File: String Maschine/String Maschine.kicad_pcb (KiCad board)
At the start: 2 copper layers, 40 parts, among them J1 Conn_01x03_Male, U1 LM358, U2 4069, U3 LM358, U4 LM317_TO-220, U5 MN3209, U6 LM7809_TO220, U7 4010

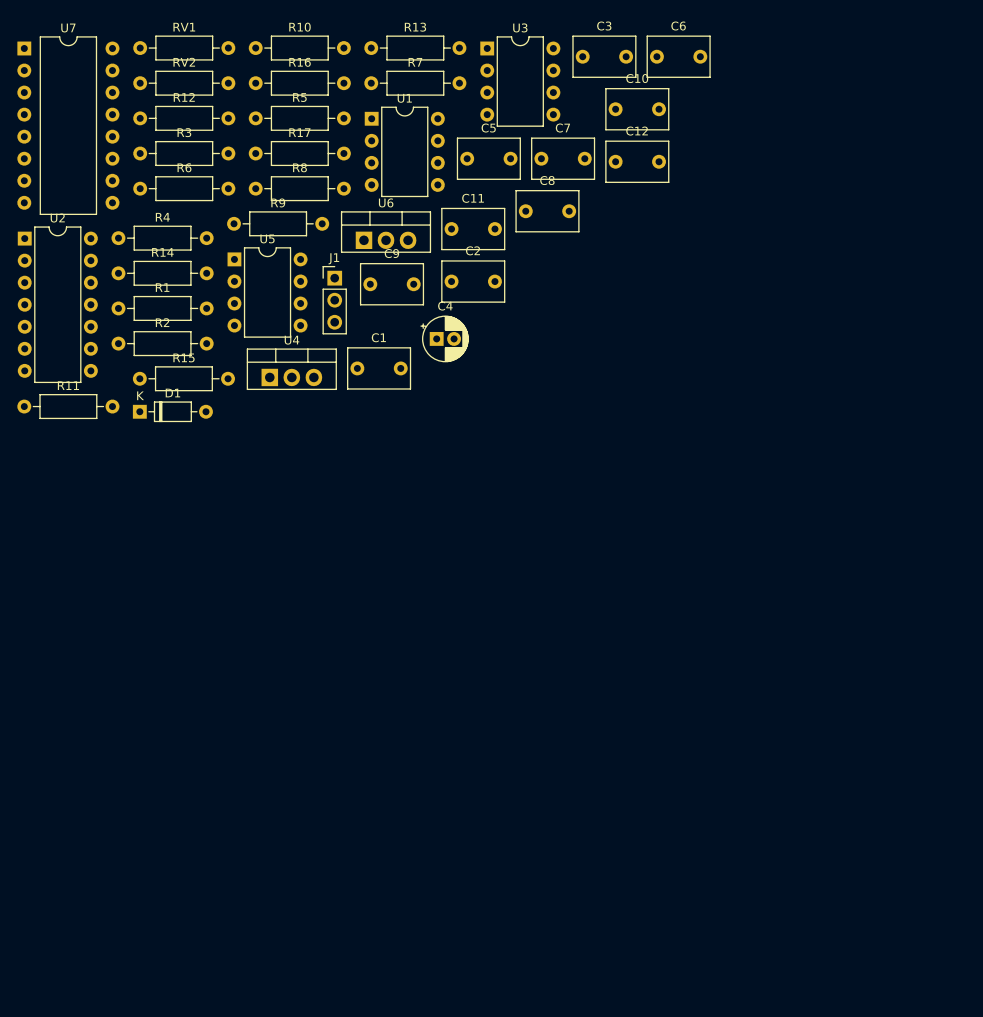
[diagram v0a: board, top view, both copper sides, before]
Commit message: String Maschine - assign symbols
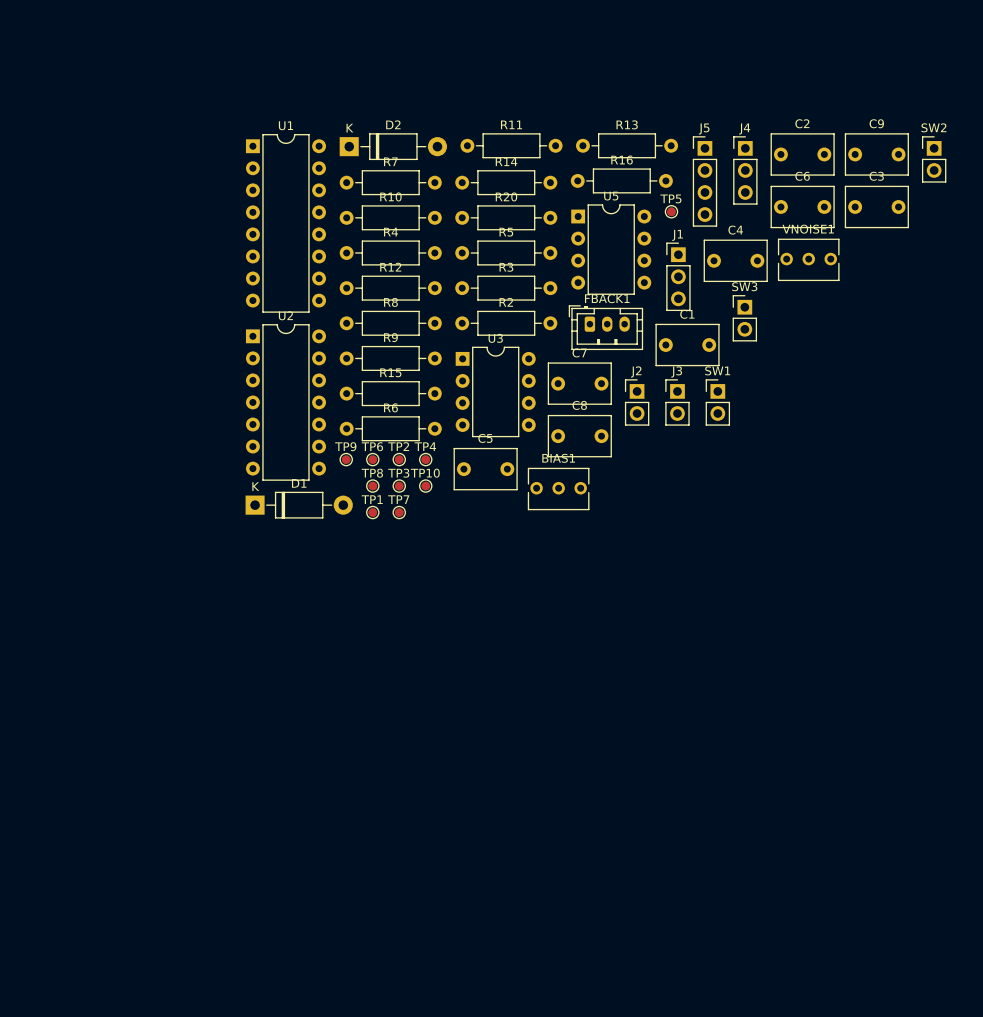
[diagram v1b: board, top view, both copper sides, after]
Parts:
- removed C10, C11: 3.3n, Capacitor_THT:C_Rect_L7.0mm_W4.5mm_P5.00mm
- removed C12: 220n, Capacitor_THT:C_Rect_L7.0mm_W4.5mm_P5.00mm
- removed R1: 10k, Resistor_THT:R_Axial_DIN0207_L6.3mm_D2.5mm_P10.16mm_Horizontal
- removed R17, RV2: 100k, Resistor_THT:R_Axial_DIN0207_L6.3mm_D2.5mm_P10.16mm_Horizontal
- removed RV1: 2k, Resistor_THT:R_Axial_DIN0207_L6.3mm_D2.5mm_P10.16mm_Horizontal
- removed U4: LM317_TO-220, Package_TO_SOT_THT:TO-220-3_Vertical
- removed U6: LM7809_TO220, Package_TO_SOT_THT:TO-220-3_Vertical
- removed U7: 4010, Package_DIP:DIP-16_W10.16mm
- added BIAS1: 100k, Potentiometer_THT:Potentiometer_Bourns_3266Y_Vertical, F.Cu at (122.5, 90.0)
- added D2: 1N47xxA, Diode_THT:D_DO-41_SOD81_P10.16mm_Horizontal, F.Cu at (95.8, 50.6)
- added FBACK1: 100k, Connector_JST:JST_PH_B3B-PH-K_1x03_P2.00mm_Vertical, F.Cu at (123.6, 71.1)
- added J2: VGG, Connector_PinHeader_2.54mm:PinHeader_1x02_P2.54mm_Vertical, F.Cu at (129.0, 78.8)
- added J3: VOut, Connector_PinHeader_2.54mm:PinHeader_1x02_P2.54mm_Vertical, F.Cu at (133.7, 78.8)
- added J4: Vin, Connector_PinHeader_2.54mm:PinHeader_1x03_P2.54mm_Vertical, F.Cu at (141.5, 50.9)
- added J5: CTLS, Connector_PinHeader_2.54mm:PinHeader_1x04_P2.54mm_Vertical, F.Cu at (136.8, 50.9)
- added R20: 10k, Resistor_THT:R_Axial_DIN0207_L6.3mm_D2.5mm_P10.16mm_Horizontal, F.Cu at (108.8, 58.9)
- added SW1: FBACK, Connector_PinHeader_2.54mm:PinHeader_1x02_P2.54mm_Vertical, F.Cu at (138.3, 78.8)
- added SW2: NOISE, Connector_PinHeader_2.54mm:PinHeader_1x02_P2.54mm_Vertical, F.Cu at (163.2, 50.9)
- added SW3: FBACK, Connector_PinHeader_2.54mm:PinHeader_1x02_P2.54mm_Vertical, F.Cu at (141.4, 69.2)
- added TP1: NIn, TestPoint:TestPoint_Pad_D1.0mm, F.Cu at (98.5, 92.8)
- added TP10: DELAY, TestPoint:TestPoint_Pad_D1.0mm, F.Cu at (104.7, 89.8)
- added TP2: VCF, TestPoint:TestPoint_Pad_D1.0mm, F.Cu at (101.6, 86.7)
- added TP3: VGG, TestPoint:TestPoint_Pad_D1.0mm, F.Cu at (101.6, 89.8)
- added TP4: VBIAS, TestPoint:TestPoint_Pad_D1.0mm, F.Cu at (104.7, 86.7)
- added TP5: CP2, TestPoint:TestPoint_Pad_D1.0mm, F.Cu at (133.0, 58.1)
- added TP6: CP1, TestPoint:TestPoint_Pad_D1.0mm, F.Cu at (98.5, 86.7)
- added TP7: CVF, TestPoint:TestPoint_Pad_D1.0mm, F.Cu at (101.6, 92.8)
- added TP8: CVN, TestPoint:TestPoint_Pad_D1.0mm, F.Cu at (98.5, 89.8)
- added TP9: GND, TestPoint:TestPoint_Pad_D1.0mm, F.Cu at (95.5, 86.7)
- added VNOISE1: 100k, Potentiometer_THT:Potentiometer_Bourns_3266Y_Vertical, F.Cu at (151.3, 63.6)
- C1: value 330n -> 220n
- C2: value 100n -> 560p
- C3: value 220n -> 470p
- C4: value 47u -> 560p; footprint Capacitor_THT:CP_Radial_D5.0mm_P2.00mm -> Capacitor_THT:C_Rect_L7.0mm_W4.5mm_P5.00mm
- C5: value 3.3n -> 470p
- C6: value 3.3n -> 560p
- C9: value 3.3n -> 1u
- D1: value BZX55C4V7 -> 1N47xxA; footprint Diode_THT:D_DO-35_SOD27_P7.62mm_Horizontal -> Diode_THT:D_DO-41_SOD81_P10.16mm_Horizontal
- J1: value Conn_01x03_Male -> Vin
- R14, R16, R5, R6: value 47k -> 27k
- R15: value 47k -> 470
- R2: value 1k -> 27k
- R3: value 10k -> 470
- R4: value 10k -> 27k
- R7: value 100k -> 470
- R8, R9: value 100k -> 27k
- U1: value LM358 -> v2164; footprint Package_DIP:DIP-8_W7.62mm -> Package_DIP:DIP-16_W7.62mm
- U2: value 4069 -> LM324
- U3: value LM358 -> Pentanoise
- moved R11 59.2 mm to (109.5, 50.5)
- moved C9 57.8 mm to (154.1, 51.5)
- moved R14 40.9 mm to (108.8, 54.8)
- moved C2 40.7 mm to (145.6, 51.5)
- moved R3 40.2 mm to (108.8, 67.0)
- moved U5 39.9 mm to (122.2, 58.7)
- moved J1 39.7 mm to (133.8, 63.1)
- moved R2 39.7 mm to (108.8, 71.0)
- moved R16 38.8 mm to (122.2, 54.6)
- moved R6 36.5 mm to (95.5, 83.2)
- moved U3 35.9 mm to (108.9, 75.1)
- moved C3 35.8 mm to (154.1, 57.6)
- moved C5 35.8 mm to (109.0, 87.8)
- moved C1 35.6 mm to (132.3, 73.5)
- moved C4 33.2 mm to (137.9, 63.8)
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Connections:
- C1 pad 1: GND -> Net-(C1-Pad1)
- C1 pad 2: +12V -> Net-(C1-Pad2)
- C2 pad 2: +9V -> Net-(C2-Pad2)
- C3 pad 1: FXIn -> Net-(C3-Pad1)
- C4 pad 1: +4V5 -> GND
- C4 pad 2: GND -> Net-(C4-Pad2)
- C5 pad 1: GND -> Net-(C5-Pad1)
- C9 pad 1: GND -> Net-(R20-Pad2)
- C9 pad 2: Net-(C9-Pad2) -> Net-(U5-Pad3)
- D1 pad 1: Net-(R2-Pad1) -> +5V
- D1 pad 2: GND -> Net-(U5-Pad3)
- J1 pad 1: Net-(J1-Pad1) -> -5V
- J1 pad 3: +3V3 -> +5V
- R14 pad 1: Net-(C8-Pad2) -> Net-(R14-Pad1)
- R14 pad 2: Net-(C9-Pad2) -> Net-(C8-Pad2)
- R15 pad 1: Net-(C9-Pad2) -> Net-(R15-Pad1)
- R15 pad 2: Net-(C10-Pad2) -> Net-(C6-Pad2)
- R16 pad 1: Net-(C10-Pad2) -> Net-(R16-Pad1)
- R16 pad 2: Net-(C11-Pad2) -> Net-(R15-Pad1)
- R2 pad 2: +9V -> Net-(C1-Pad2)
- R3 pad 1: Net-(R1-Pad2) -> Net-(R2-Pad1)
- R3 pad 2: Net-(R3-Pad2) -> Net-(C2-Pad2)
- R4 pad 1: Net-(R2-Pad1) -> Net-(R4-Pad1)
- R4 pad 2: +4V5 -> Net-(R4-Pad2)
- R5 pad 1: Net-(R3-Pad2) -> Net-(R20-Pad2)
- R5 pad 2: Net-(C5-Pad2) -> Net-(R4-Pad1)
- R6 pad 1: Net-(C5-Pad2) -> Net-(R6-Pad1)
- R6 pad 2: Net-(C6-Pad2) -> Net-(C3-Pad1)
- R7 pad 1: Net-(C6-Pad2) -> Net-(R6-Pad1)
- R7 pad 2: Net-(R7-Pad2) -> Net-(C4-Pad2)
- R8 pad 1: Net-(C6-Pad2) -> Net-(C5-Pad1)
- R8 pad 2: Net-(R8-Pad2) -> Net-(R6-Pad1)
- R9 pad 1: Net-(R7-Pad2) -> Net-(R15-Pad1)
- R9 pad 2: Net-(C7-Pad1) -> Net-(C5-Pad1)
- U1 pad 1: Net-(R3-Pad2) -> unconnected-(U1-Pad1)
- U1 pad 2: Net-(R1-Pad2) -> Net-(R15-Pad1)
- U1 pad 3: +4V5 -> CVF
- U1 pad 4: GND -> Net-(C5-Pad2)
- U1 pad 5: +4V5 -> Net-(C3-Pad2)
- U1 pad 6: Net-(C6-Pad2) -> CVF
- U1 pad 7: Net-(R8-Pad2) -> Net-(R6-Pad1)
- U1 pad 8: +9V -> GND
- U2 pad 1: CP1 -> Net-(C5-Pad1)
- U2 pad 10: unconnected-(U2-Pad10) -> GND
- U2 pad 11: GND -> -5V
- U2 pad 12: unconnected-(U2-Pad12) -> GND
- U2 pad 13: GND -> Net-(R14-Pad1)
- U2 pad 14: +9V -> Net-(C7-Pad1)
- U2 pad 2: CP2 -> Net-(C5-Pad2)
- U2 pad 4: unconnected-(U2-Pad4) -> +5V
- U2 pad 6: unconnected-(U2-Pad6) -> Net-(C3-Pad2)
- U2 pad 7: GND -> Net-(C3-Pad1)
- U2 pad 8: unconnected-(U2-Pad8) -> Net-(R20-Pad2)
- U2 pad 9: GND -> Net-(R4-Pad1)
- U3 pad 1: Net-(C12-Pad1) -> +5V
- U3 pad 2: Net-(C11-Pad2) -> unconnected-(U3-Pad2)
- U3 pad 3: +4V5 -> unconnected-(U3-Pad3)
- U3 pad 4: GND -> (no net)
- U3 pad 5: +4V5 -> unconnected-(U3-Pad5)
- U3 pad 6: Net-(C7-Pad1) -> unconnected-(U3-Pad6)
- U3 pad 7: Net-(R7-Pad2) -> Net-(VNOISE1-Pad1)
- U3 pad 8: +9V -> GND
- U5 pad 3: Net-(R8-Pad2) -> Net-(U5-Pad3)
- U5 pad 4: /+8.4V  -> VGG
- U5 pad 5: +9V -> +5V

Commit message: String Maschine - finish voice board
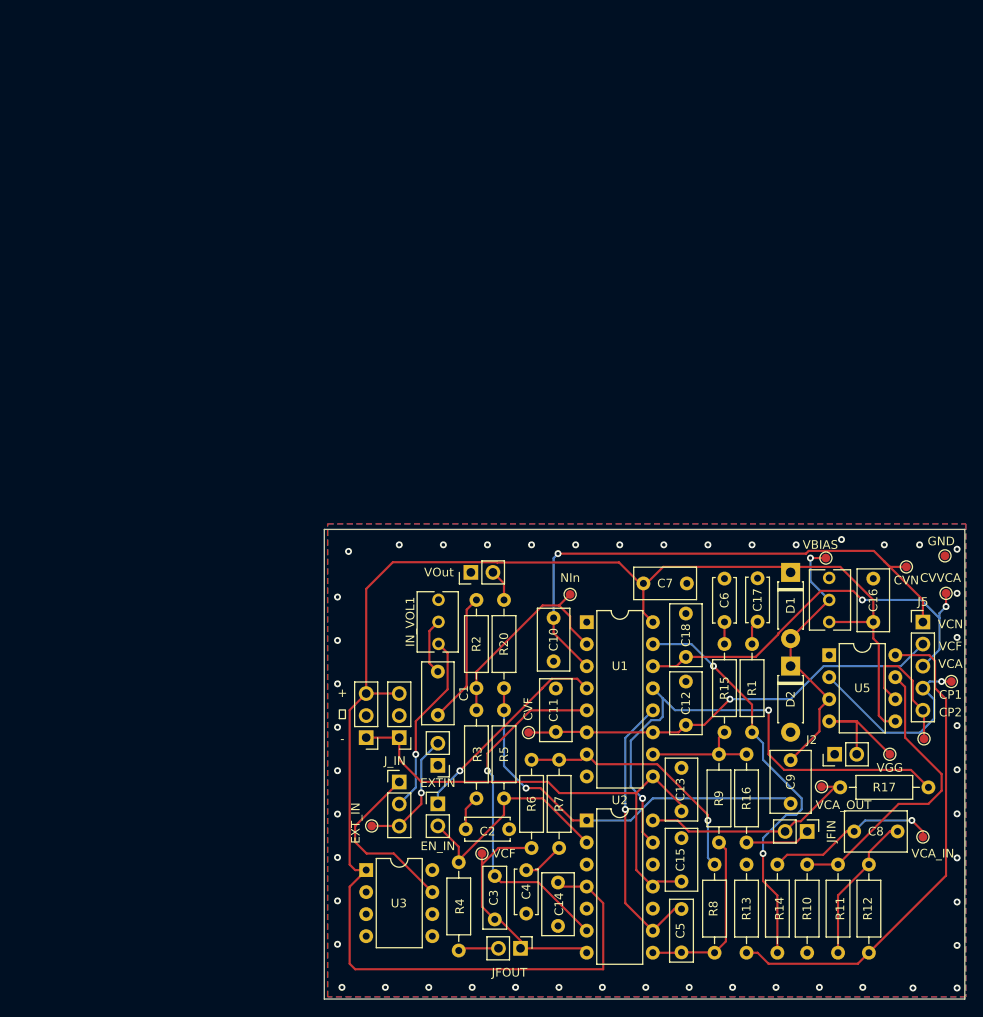
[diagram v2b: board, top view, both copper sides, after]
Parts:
- removed FBACK1: 100k, Connector_JST:JST_PH_B3B-PH-K_1x03_P2.00mm_Vertical
- removed VNOISE1: 100k, Potentiometer_THT:Potentiometer_Bourns_3266Y_Vertical
- added C10: 220n, Capacitor_THT:C_Rect_L7.0mm_W3.5mm_P5.00mm, F.Cu at (119.4, 109.9)
- added C11: 220n, Capacitor_THT:C_Rect_L7.0mm_W3.5mm_P5.00mm, F.Cu at (119.6, 113.1)
- added C12: 220n, Capacitor_THT:C_Rect_L7.0mm_W3.5mm_P5.00mm, F.Cu at (134.6, 112.3)
- added C13: 100n, Capacitor_THT:C_Rect_L7.0mm_W3.5mm_P5.00mm, F.Cu at (134.1, 127.2)
- added C14: 100n, Capacitor_THT:C_Rect_L7.0mm_W3.5mm_P5.00mm, F.Cu at (119.9, 135.4)
- added C15: 100n, Capacitor_THT:C_Rect_L7.0mm_W3.5mm_P5.00mm, F.Cu at (134.1, 135.3)
- added C16: 100n, Capacitor_THT:C_Rect_L7.0mm_W3.5mm_P5.00mm, F.Cu at (156.2, 105.4)
- added C17: 560p, Capacitor_THT:C_Disc_D5.0mm_W2.5mm_P5.00mm, F.Cu at (142.9, 100.4)
- added C18: 220n, Capacitor_THT:C_Rect_L7.0mm_W3.5mm_P5.00mm, F.Cu at (134.6, 104.4)
- added IN1: J_IN, Connector_PinHeader_2.54mm:PinHeader_1x03_P2.54mm_Vertical, F.Cu at (101.6, 123.8)
- added IN_VOL1: 100k, Potentiometer_THT:Potentiometer_Bourns_3266Y_Vertical, F.Cu at (106.1, 107.9)
- added J6: EXTIN, Connector_PinHeader_2.54mm:PinHeader_1x02_P2.54mm_Vertical, F.Cu at (106.0, 121.9)
- added R1: 470, Resistor_THT:R_Axial_DIN0207_L6.3mm_D2.5mm_P10.16mm_Horizontal, F.Cu at (142.2, 118.1)
- added R17: 27k, Resistor_THT:R_Axial_DIN0207_L6.3mm_D2.5mm_P10.16mm_Horizontal, F.Cu at (152.4, 124.5)
- added TP11: EXT_IN, TestPoint:TestPoint_Pad_D1.0mm, F.Cu at (98.4, 128.9)
- added TP12: CVVCA, TestPoint:TestPoint_Pad_D1.0mm, F.Cu at (164.6, 102.1)
- added TP13: VCA_IN, TestPoint:TestPoint_Pad_D1.0mm, F.Cu at (161.9, 130.2)
- C1: footprint Capacitor_THT:C_Rect_L7.0mm_W4.5mm_P5.00mm -> Capacitor_THT:C_Rect_L7.0mm_W3.5mm_P5.00mm
- C2, C4, C6: footprint Capacitor_THT:C_Rect_L7.0mm_W4.5mm_P5.00mm -> Capacitor_THT:C_Disc_D5.0mm_W2.5mm_P5.00mm
- C3, C5: value 470p -> 1.2n; footprint Capacitor_THT:C_Rect_L7.0mm_W4.5mm_P5.00mm -> Capacitor_THT:C_Rect_L7.0mm_W2.5mm_P5.00mm
- C7: value 220n -> 100n; footprint Capacitor_THT:C_Rect_L7.0mm_W4.5mm_P5.00mm -> Capacitor_THT:C_Rect_L7.0mm_W3.5mm_P5.00mm
- D1, D2: footprint Diode_THT:D_DO-41_SOD81_P10.16mm_Horizontal -> Diode_THT:D_DO-41_SOD81_P7.62mm_Horizontal
- J5: footprint Connector_PinHeader_2.54mm:PinHeader_1x04_P2.54mm_Vertical -> Connector_PinHeader_2.54mm:PinHeader_1x05_P2.54mm_Vertical
- SW1: value FBACK -> JFOUT
- SW2: value NOISE -> EN_IN
- SW3: value FBACK -> JFIN
- TP10: value DELAY -> VCA_OUT
- TP5: value CP2 -> CP1
- TP6: value CP1 -> CP2
- moved R10 99.9 mm to (148.6, 143.5), turned to 90 degrees
- moved R14 95.9 mm to (145.2, 143.5), turned to 90 degrees
- moved R13 94.9 mm to (141.6, 143.5), turned to 90 degrees
- moved SW2 94.7 mm to (106.0, 126.4)
- moved R11 93.2 mm to (152.1, 133.3), turned to -90 degrees
- moved C3 92.0 mm to (112.6, 139.7), turned to 90 degrees
- moved R12 89.6 mm to (155.7, 133.3), turned to -90 degrees
- moved R8 84.0 mm to (137.9, 143.5), turned to 90 degrees
- moved C2 83.8 mm to (114.3, 129.3), turned to 180 degrees
- moved J4 80.7 mm to (97.8, 118.7), turned to 180 degrees
- moved R16 78.7 mm to (141.6, 130.8), turned to 90 degrees
- moved D2 78.5 mm to (146.7, 110.5), turned to -90 degrees
- moved C4 78.2 mm to (116.2, 139.0), turned to 90 degrees
- moved C9 75.1 mm to (146.7, 126.3), turned to 90 degrees
- moved R4 71.4 mm to (108.5, 133.1), turned to -90 degrees
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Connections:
- C7 pad 1: Net-(C7-Pad1) -> GND
- C7 pad 2: Net-(C7-Pad2) -> +5V
- C9 pad 1: Net-(R20-Pad2) -> Net-(C9-Pad1)
- J5 pad 3: CP1 -> CVVCA
- J5 pad 4: CP2 -> CP1
- R14 pad 1: Net-(R14-Pad1) -> Net-(R1-Pad1)
- R20 pad 2: Net-(R20-Pad2) -> Net-(C9-Pad1)
- R5 pad 1: Net-(R20-Pad2) -> Net-(C9-Pad1)
- SW2 pad 1: Net-(U1-Pad13) -> Net-(SW2-Pad1)
- SW3 pad 2: Net-(C7-Pad2) -> Net-(R17-Pad1)
- TP10 pad 1: Net-(C7-Pad2) -> Net-(R17-Pad1)
- U1 pad 10: GND -> Net-(R15-Pad1)
- U1 pad 11: GND -> CVF
- U1 pad 12: unconnected-(U1-Pad12) -> Net-(C5-Pad2)
- U1 pad 13: Net-(U1-Pad13) -> Net-(R17-Pad2)
- U1 pad 14: CVN -> CVVCA
- U1 pad 15: Net-(R2-Pad1) -> Net-(R1-Pad1)
- U1 pad 2: Net-(R15-Pad1) -> Net-(R2-Pad1)
- U1 pad 3: CVF -> CVN
- U1 pad 4: Net-(C5-Pad2) -> Net-(SW2-Pad1)
- U2 pad 1: Net-(C5-Pad1) -> Net-(C9-Pad1)
- U2 pad 13: Net-(R14-Pad1) -> Net-(R17-Pad2)
- U2 pad 14: Net-(C7-Pad1) -> Net-(R17-Pad1)
- U2 pad 2: Net-(C5-Pad2) -> Net-(R4-Pad1)
- U2 pad 8: Net-(R20-Pad2) -> Net-(C5-Pad1)
- U2 pad 9: Net-(R4-Pad1) -> Net-(C5-Pad2)
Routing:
- net +5V: track 0.00 -> 182.7 mm
- net CVN: track 0.00 -> 64.6 mm, vias 0 -> 1
- net Net-(R17-Pad2): track 0.00 -> 59.0 mm, vias 0 -> 2
- net -5V: track 0.00 -> 58.4 mm
- net Net-(R12-Pad2): track 0.00 -> 57.8 mm
- net CVF: track 0.00 -> 49.7 mm, vias 0 -> 1
- net Net-(R1-Pad1): track 0.00 -> 48.4 mm, vias 0 -> 2
- net CVVCA: track 0.00 -> 47.5 mm, vias 0 -> 2
- net Net-(C9-Pad1): track 0.00 -> 45.9 mm, vias 0 -> 1
- net Net-(C3-Pad2): track 0.00 -> 41.2 mm, vias 0 -> 1
- net Net-(R10-Pad2): track 0.00 -> 34.3 mm
- net Net-(C5-Pad2): track 0.00 -> 32.4 mm, vias 0 -> 1
- net Net-(BIAS1-Pad2): track 0.00 -> 31.8 mm, vias 0 -> 1
- net Net-(R6-Pad1): track 0.00 -> 29.5 mm, vias 0 -> 1
- net Net-(C3-Pad1): track 0.00 -> 27.4 mm
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- added copper zone on B.Cu, net GND
- added copper zone on F.Cu, net GND
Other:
- board outline added: 73.8 x 54.1 mm
- board text added: "+"
- board text added: "-"
- board text added: "VCA"
- board text added: "VCF"
- board text added: "VCN"
- board text added: "⏚"
